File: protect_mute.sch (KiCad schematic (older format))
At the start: 40 parts, among them K1 G5LE-1, K2 G5LE-1, Q1 BC546, Q2 BC556, Q3 BC546, Q4 BD140

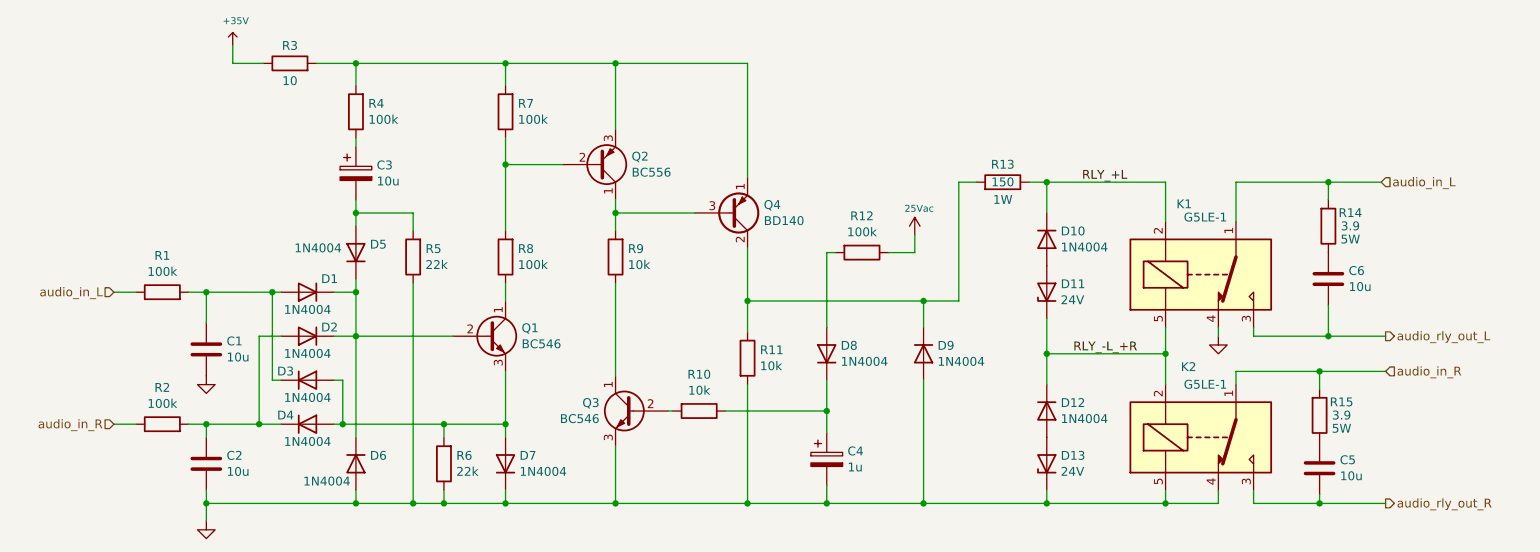
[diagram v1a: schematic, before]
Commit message: Lots of part changes to SMD devices. Adding MPN, MFG to all parts for BOM export.
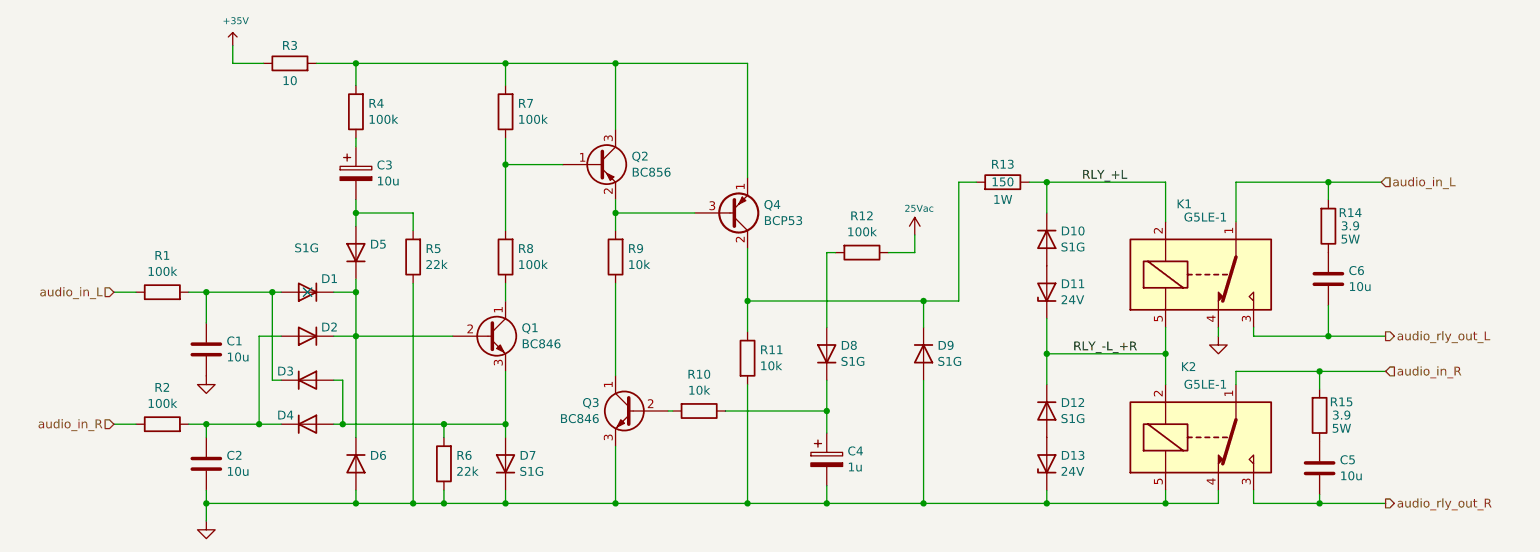
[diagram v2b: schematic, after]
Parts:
- removed Q2: BC556, Package_TO_SOT_THT:TO-92_Inline, symbol Transistor_BJT:BC556
- added Q2: BC856, Package_TO_SOT_SMD:SOT-23, symbol Transistor_BJT:BC856
- C1, C2, C5, C6: footprint Capacitor_SMD:C_1206_3216Metric_Pad1.42x1.75mm_HandSolder -> Capacitor_SMD:C_1206_3216Metric; MFG (none) -> Murata Electronics; MPN (none) -> GRT31CR61H106KE01L
- C3: footprint Capacitor_THT:CP_Radial_D5.0mm_P2.00mm -> Capacitor_SMD:CP_Elec_5x3; DigiKey (none) -> https://www.digikey.com/product-detail/en/w%C3%BCrth-elektr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; MFG (none) -> Würth Elektronik; MPN (none) -> 865080642006
- C4: footprint Capacitor_THT:CP_Radial_D5.0mm_P2.00mm -> Capacitor_SMD:CP_Elec_4x5.4; DigiKey (none) -> https://www.digikey.com/product-detail/en/w%C3%BCrth-elektr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; MFG (none) -> Würth Elektronik; MPN (none) -> 865060640001
- D1, D10, D12, D2, D3, D4, D5, D6, D7, D8, D9: value 1N4004 -> S1G; footprint Diode_THT:D_DO-41_SOD81_P10.16mm_Horizontal -> Diode_SMD:D_SMA; DigiKey (none) -> https://www.digikey.com/product-detail/en/on-semiconductor/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; MFG (none) -> ON Semiconductor; MPN (none) -> S1G
- D11, D13: DigiKey (none) -> https://www.digikey.com/product-detail/en/on-semiconductor/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; MFG (none) -> ON Semiconductor; MPN (none) -> 1SMA5934BT3G
- K1, K2: DigiKey (none) -> https://www.digikey.com/product-detail/en/omron-electronics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; MFG (none) -> Omron Electronics Inc-EMC Div; MPN (none) -> G5LE-1-VDDC12
- Q1, Q3: value BC546 -> BC846; footprint Package_TO_SOT_THT:TO-92_Inline -> Package_TO_SOT_SMD:SOT-23; DigiKey (none) -> https://www.digikey.com/product-detail/en/on-semiconductor/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; MFG (none) -> ON Semiconductor; MPN (none) -> BC846BLT1G
- Q4: value BD140 -> BCP53; footprint Package_TO_SOT_THT:TO-126-3_Vertical -> Package_TO_SOT_SMD:SOT-223; DigiKey (none) -> https://www.digikey.com/product-detail/en/on-semiconductor/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; MFG (none) -> ON Semiconductor; MPN (none) -> SBCP53-10T1G
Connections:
- net at Q4.3 (B), R9.2: now also Q2.2 (E)
- net at R7.1, R8.2: now also Q2.1 (B)
- net at Q4.1 (E), R3.2, R4.2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: now also Q2.3 (C)
- no-connect marks 0 -> 1

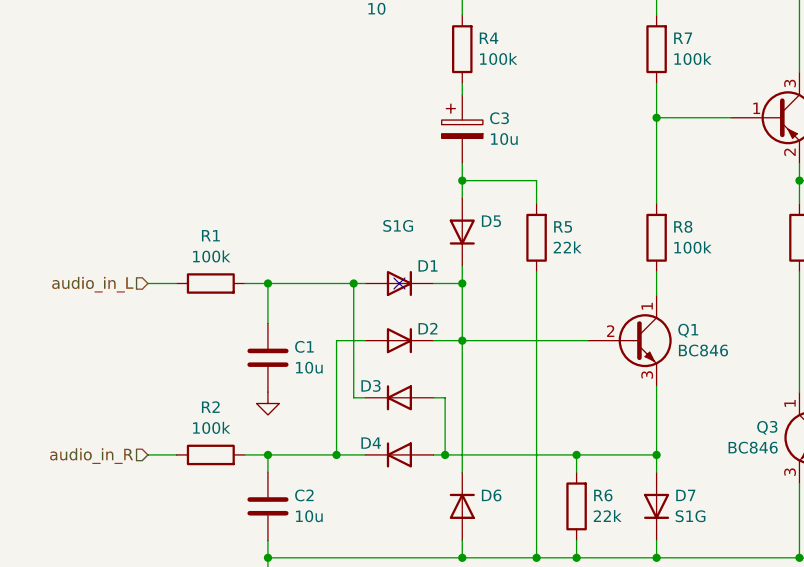
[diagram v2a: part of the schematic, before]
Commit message: Layout startover, sorting, some routing. Removed redundant fuses. BOM export.
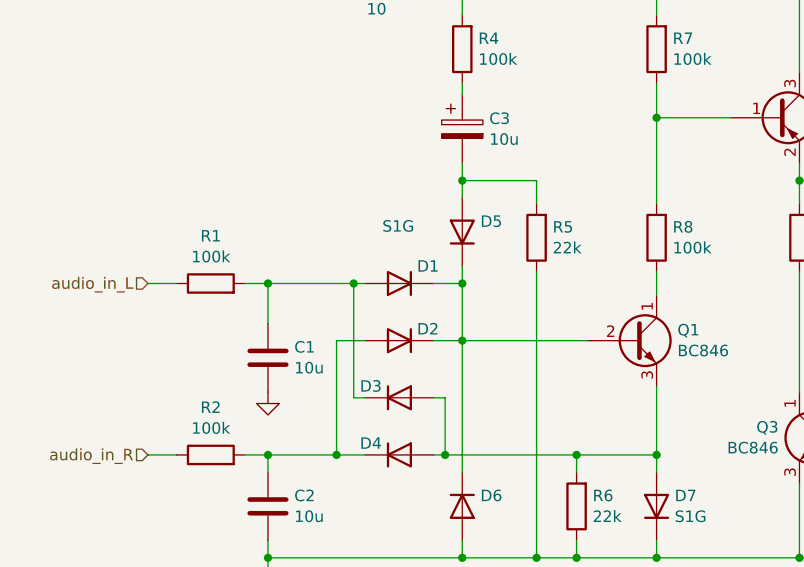
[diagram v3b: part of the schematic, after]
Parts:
- C3, C4: MFG Würth Elektronik -> Wurth Elektronik
- R1, R12, R2, R4, R7, R8: DigiKey (none) -> https://www.digikey.com/product-detail/en/vishay-beyschlag/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; MFG (none) -> Vishay Beyschlag; MPN (none) -> MCT06030C1003FP500
- R10, R11, R9: DigiKey (none) -> https://www.digikey.com/product-detail/en/te-connectivity-p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; MFG (none) -> TE Connectivity Passive Product; MPN (none) -> CRGCQ0603F10K
- R13: footprint Resistor_THT:R_Axial_DIN0207_L6.3mm_D2.5mm_P7.62mm_Horizontal -> Resistor_SMD:R_2512_6332Metric; DigiKey https://www.digikey.com/product-detail/en/yageo/FMP100JR-52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 -> https://www.digikey.com/product-detail/en/vishay-dale/CRCW2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; MFG (none) -> Vishay Dale; MPN (none) -> CRCW2512150RFKEG
- R14, R15: footprint Resistor_THT:R_Axial_Power_L25.0mm_W9.0mm_P10.16mm_Vertical -> Resistor_THT:R_Axial_DIN0918_L18.0mm_D9.0mm_P7.62mm_Vertical; DigiKey https://www.digikey.com/product-detail/en/vishay-bc-compone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 -> https://www.digikey.com/product-detail/en/te-connectivity-p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; MFG (none) -> TE Connectivity Passive Product; MPN (none) -> SQPW53R9J
- R3: DigiKey (none) -> https://www.digikey.com/product-detail/en/panasonic-electro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; MFG (none) -> Panasonic Electronic Components; MPN (none) -> ERJ-PA3F10R0V
- R5, R6: DigiKey (none) -> https://www.digikey.com/product-detail/en/te-connectivity-p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; MFG (none) -> TE Connectivity Passive Product; MPN (none) -> CRGCQ0603F22K
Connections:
- no-connect marks 1 -> 0
